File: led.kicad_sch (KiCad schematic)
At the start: 2 parts

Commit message: [FIX](General) footprints
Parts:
- renumbered D3 to D4
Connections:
- net VDD renamed VCC

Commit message: [ADD](General) added all footprints expect leds
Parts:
- C20: footprint (none) -> Capacitor_SMD:C_0603_1608Metric_Pad1.08x0.95mm_HandSolder
- D4: footprint kicad-keyboard-parts:MX_SK6812MINI-E -> LED_SMD:LED_SK6812MINI_PLCC4_3.5x3.5mm_P1.75mm
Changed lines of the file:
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@@
 			)
 		)
-		(property "Footprint" "kicad-keyboard-parts:MX_SK6812MINI-E"
+		(property "Footprint" "LED_SMD:LED_SK6812MINI_PLCC4_3.5x3.5mm_P1.75mm"
 			(at 134.62 102.87 0)
 			(effects
@@
 			)
 		)
-		(property "Footprint" ""
+		(property "Footprint" "Capacitor_SMD:C_0603_1608Metric_Pad1.08x0.95mm_HandSolder"
 			(at 123.19 83.5152 0)
 			(effects

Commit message: [ADD](General) added all footprints
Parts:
- D4: footprint LED_SMD:LED_SK6812MINI_PLCC4_3.5x3.5mm_P1.75mm -> kicad-keyboard-parts:MX_SK6812MINI-E_REV
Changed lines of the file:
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@@
 			)
 		)
-		(property "Footprint" "LED_SMD:LED_SK6812MINI_PLCC4_3.5x3.5mm_P1.75mm"
+		(property "Footprint" "kicad-keyboard-parts:MX_SK6812MINI-E_REV"
 			(at 134.62 102.87 0)
 			(effects

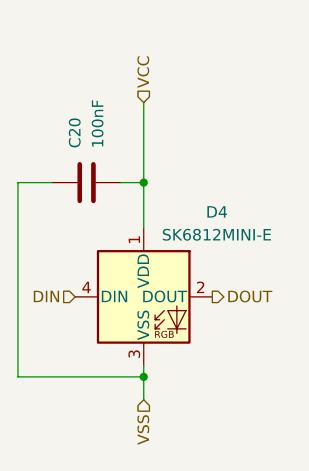
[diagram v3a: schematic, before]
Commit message: [FIX](USB) main usb net labels
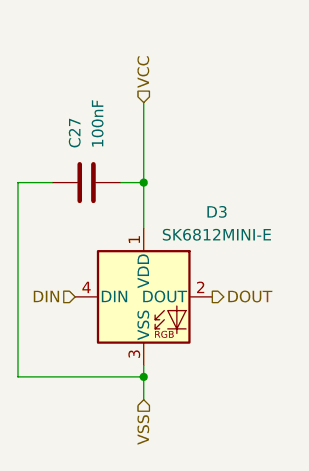
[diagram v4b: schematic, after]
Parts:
- renumbered C20 to C27, D4 to D3

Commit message: [UPDATE](PCB) placed LEDs
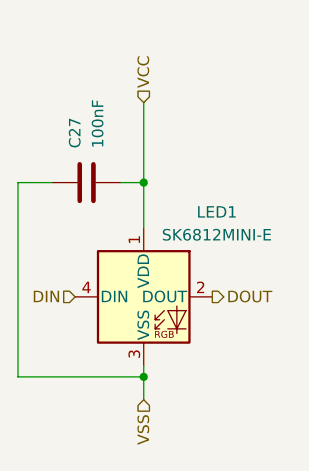
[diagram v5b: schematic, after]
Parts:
- renumbered D3 to LED1
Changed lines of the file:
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@@
 		(on_board yes)
 		(dnp no)
-		(property "Reference" "D3"
+		(property "Reference" "LED1"
 			(at 141.478 85.852 0)
 			(effects
@@
 			(project "RyzzenKeyboard"
 				(path "/5d44d704-6136-40a8-98a4-93f001ea8743/ddd39123-7c60-4daf-80ad-ae6eff6f8029/0399f5c2-9535-4061-916d-b5ef4d4709ef"
-					(reference "D31")
+					(reference "LED27")
 					(unit 1)
 				)
 				(path "/5d44d704-6136-40a8-98a4-93f001ea8743/ddd39123-7c60-4daf-80ad-ae6eff6f8029/1150627b-b8e0-4222-bb46-910bf944c460"
-					(reference "D24")
+					(reference "LED20")
 					(unit 1)
 				)
 				(path "/5d44d704-6136-40a8-98a4-93f001ea8743/ddd39123-7c60-4daf-80ad-ae6eff6f8029/129c2b3f-4234-4485-9309-c3a009b76647"
-					(reference "D9")
+					(reference "LED6")
 					(unit 1)
 				)
 				(path "/5d44d704-6136-40a8-98a4-93f001ea8743/ddd39123-7c60-4daf-80ad-ae6eff6f8029/23035616-5bf6-4409-a235-197278ce7640"
-					(reference "D7")
+					(reference "LED4")
 					(unit 1)
 				)
 				(path "/5d44d704-6136-40a8-98a4-93f001ea8743/ddd39123-7c60-4daf-80ad-ae6eff6f8029/2450ef32-9076-405c-ad54-6d129acff93d"
-					(reference "D14")
+					(reference "LED11")
 					(unit 1)
 				)
 				(path "/5d44d704-6136-40a8-98a4-93f001ea8743/ddd39123-7c60-4daf-80ad-ae6eff6f8029/29d75898-dcbd-4cda-88aa-9921bb8ce3e1"
-					(reference "D4")
+					(reference "LED2")
 					(unit 1)
 				)
 				(path "/5d44d704-6136-40a8-98a4-93f001ea8743/ddd39123-7c60-4daf-80ad-ae6eff6f8029/2af18925-a967-4b19-b674-45c1df568138"
-					(reference "D36")
+					(reference "LED32")
 					(unit 1)
 				)
 				(path "/5d44d704-6136-40a8-98a4-93f001ea8743/ddd39123-7c60-4daf-80ad-ae6eff6f8029/487bf992-d807-4e8f-b1c4-66d16985b269"
-					(reference "D6")
+					(reference "LED3")
 					(unit 1)
 				)
 				(path "/5d44d704-6136-40a8-98a4-93f001ea8743/ddd39123-7c60-4daf-80ad-ae6eff6f8029/5375842c-1d17-4646-85ff-cf75bba7c088"
-					(reference "D12")
+					(reference "LED9")
 					(unit 1)
 				)
 				(path "/5d44d704-6136-40a8-98a4-93f001ea8743/ddd39123-7c60-4daf-80ad-ae6eff6f8029/561e65f5-29eb-4597-91fb-dbed31f9f730"
-					(reference "D21")
+					(reference "LED17")
 					(unit 1)
 				)
 				(path "/5d44d704-6136-40a8-98a4-93f001ea8743/ddd39123-7c60-4daf-80ad-ae6eff6f8029/6211a26f-2932-4dfd-ad2c-8cd0a7363f29"
-					(reference "D32")
+					(reference "LED28")
 					(unit 1)
 				)
 				(path "/5d44d704-6136-40a8-98a4-93f001ea8743/ddd39123-7c60-4daf-80ad-ae6eff6f8029/658ba86f-492e-41e4-bb2f-11f5138bcbb0"
-					(reference "D10")
+					(reference "LED7")
 					(unit 1)
 				)
 				(path "/5d44d704-6136-40a8-98a4-93f001ea8743/ddd39123-7c60-4daf-80ad-ae6eff6f8029/69e0cf4a-c55f-443a-9370-201bfce90350"
-					(reference "D27")
+					(reference "LED23")
 					(unit 1)
 				)
 				(path "/5d44d704-6136-40a8-98a4-93f001ea8743/ddd39123-7c60-4daf-80ad-ae6eff6f8029/710979c3-dc7f-4c61-ab43-367c4178ec26"
-					(reference "D20")
+					(reference "LED16")
 					(unit 1)
 				)
 				(path "/5d44d704-6136-40a8-98a4-93f001ea8743/ddd39123-7c60-4daf-80ad-ae6eff6f8029/75606fea-3cbb-4b03-a764-82ff74d38ad7"
-					(reference "D8")
+					(reference "LED5")
 					(unit 1)
 				)
 				(path "/5d44d704-6136-40a8-98a4-93f001ea8743/ddd39123-7c60-4daf-80ad-ae6eff6f8029/77898d4f-f711-4ecb-8b9c-12ce90ff3214"
-					(reference "D26")
+					(reference "LED22")
 					(unit 1)
 				)
 				(path "/5d44d704-6136-40a8-98a4-93f001ea8743/ddd39123-7c60-4daf-80ad-ae6eff6f8029/7c8ccf12-18cb-4416-8915-e8832372154a"
-					(reference "D35")
+					(reference "LED31")
 					(unit 1)
 				)
 				(path "/5d44d704-6136-40a8-98a4-93f001ea8743/ddd39123-7c60-4daf-80ad-ae6eff6f8029/7cf169b2-4350-4abb-8594-c9a1d272f05e"
-					(reference "D3")
+					(reference "LED1")
 					(unit 1)
 				)
 				(path "/5d44d704-6136-40a8-98a4-93f001ea8743/ddd39123-7c60-4daf-80ad-ae6eff6f8029/83601bf4-1b82-43df-b94f-0b9cf3368dc1"
-					(reference "D22")
+					(reference "LED18")
 					(unit 1)
 				)
 				(path "/5d44d704-6136-40a8-98a4-93f001ea8743/ddd39123-7c60-4daf-80ad-ae6eff6f8029/91d7ae7e-0b93-4c9f-82d5-9bb18e0876fd"
-					(reference "D34")
+					(reference "LED30")
 					(unit 1)
 				)
 				(path "/5d44d704-6136-40a8-98a4-93f001ea8743/ddd39123-7c60-4daf-80ad-ae6eff6f8029/98bd2091-6bec-4498-8c8b-90ddec18dd83"
-					(reference "D29")
+					(reference "LED25")
 					(unit 1)
 				)
 				(path "/5d44d704-6136-40a8-98a4-93f001ea8743/ddd39123-7c60-4daf-80ad-ae6eff6f8029/99751c4f-8879-48b2-80b8-b17042233be7"
-					(reference "D11")
+					(reference "LED8")
 					(unit 1)
 				)
 				(path "/5d44d704-6136-40a8-98a4-93f001ea8743/ddd39123-7c60-4daf-80ad-ae6eff6f8029/9a4fb7ce-aad0-4de0-8be8-20b04c8cbc1a"
-					(reference "D30")
+					(reference "LED26")
 					(unit 1)
 				)
 				(path "/5d44d704-6136-40a8-98a4-93f001ea8743/ddd39123-7c60-4daf-80ad-ae6eff6f8029/9f0f5370-21c8-45bd-9e77-ce861973c6b6"
-					(reference "D15")
+					(reference "LED12")
 					(unit 1)
 				)
 				(path "/5d44d704-6136-40a8-98a4-93f001ea8743/ddd39123-7c60-4daf-80ad-ae6eff6f8029/a3b2bb4f-dacd-418a-88f2-b44a3b1fcea3"
-					(reference "D28")
+					(reference "LED24")
 					(unit 1)
 				)
 				(path "/5d44d704-6136-40a8-98a4-93f001ea8743/ddd39123-7c60-4daf-80ad-ae6eff6f8029/a6a84da7-6c8f-4f5b-aa2b-5a93f9d2f50a"
-					(reference "D19")
+					(reference "LED15")
 					(unit 1)
 				)
 				(path "/5d44d704-6136-40a8-98a4-93f001ea8743/ddd39123-7c60-4daf-80ad-ae6eff6f8029/a98ee5d5-e1b0-4e3c-9aa3-6c671a342fbf"
-					(reference "D17")
+					(reference "LED14")
 					(unit 1)
 				)
 				(path "/5d44d704-6136-40a8-98a4-93f001ea8743/ddd39123-7c60-4daf-80ad-ae6eff6f8029/af5f19bb-4c6f-45b8-a600-2f0fc0e197e4"
-					(reference "D25")
+					(reference "LED21")
 					(unit 1)
 				)
 				(path "/5d44d704-6136-40a8-98a4-93f001ea8743/ddd39123-7c60-4daf-80ad-ae6eff6f8029/b030d33d-3cf0-42e2-b952-f3acdd16eaf1"
-					(reference "D33")
+					(reference "LED29")
 					(unit 1)
 				)
 				(path "/5d44d704-6136-40a8-98a4-93f001ea8743/ddd39123-7c60-4daf-80ad-ae6eff6f8029/b73c4b0d-59ba-422a-9714-ef49bda83990"
-					(reference "D13")
+					(reference "LED10")
 					(unit 1)
 				)
 				(path "/5d44d704-6136-40a8-98a4-93f001ea8743/ddd39123-7c60-4daf-80ad-ae6eff6f8029/c2e22f46-791a-4bee-bd91-e7045f65945f"
-					(reference "D16")
+					(reference "LED13")
 					(unit 1)
 				)
 				(path "/5d44d704-6136-40a8-98a4-93f001ea8743/ddd39123-7c60-4daf-80ad-ae6eff6f8029/e64fc037-d1fe-4b23-a603-e3319ec165ed"
-					(reference "D23")
+					(reference "LED19")
 					(unit 1)
 				)
@@
 				)
 				(path "/5d44d704-6136-40a8-98a4-93f001ea8743/ddd39123-7c60-4daf-80ad-ae6eff6f8029/a98ee5d5-e1b0-4e3c-9aa3-6c671a342fbf"
-					(reference "C80")
-					(unit 1)
-				)
+					(reference "C84")
+					(unit 1)
+				)

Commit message: [ADD](PCB) led and tmr caps placement
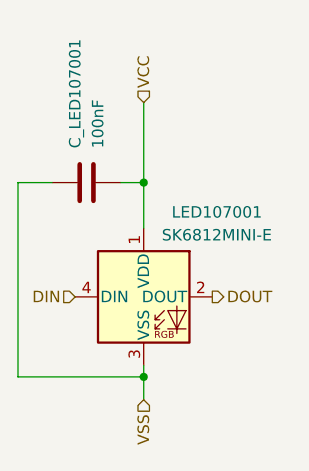
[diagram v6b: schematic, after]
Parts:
- renumbered C27 to C_LED107001, LED1 to LED107001
